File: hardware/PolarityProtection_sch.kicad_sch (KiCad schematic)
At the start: 14 parts, among them IC1 LM74502HDDFR, Q1 PSMN8R5-40MSDX

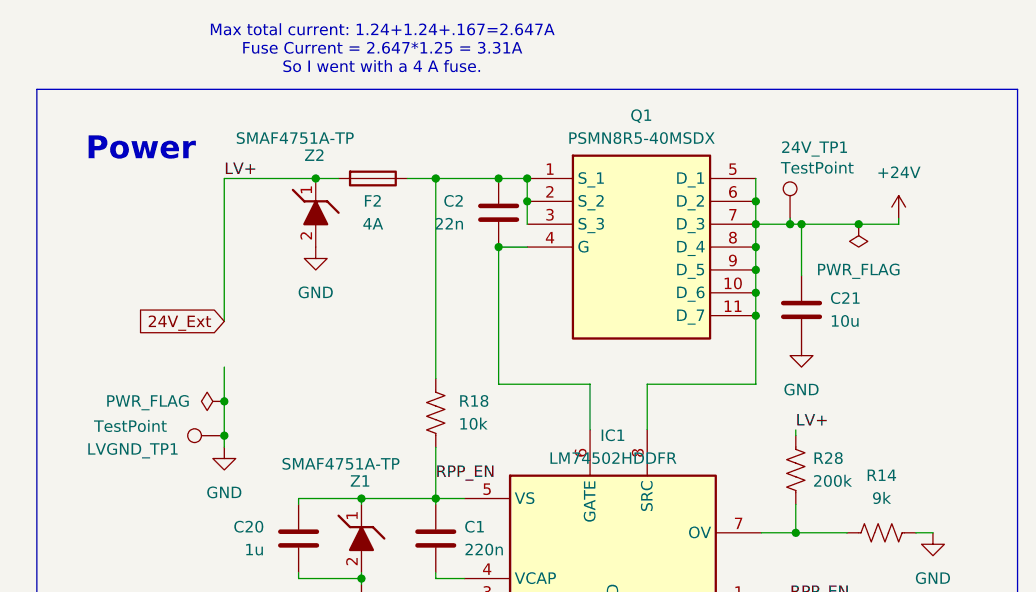
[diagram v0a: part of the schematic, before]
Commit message: Routed but having issues with gnd being pretty isolated
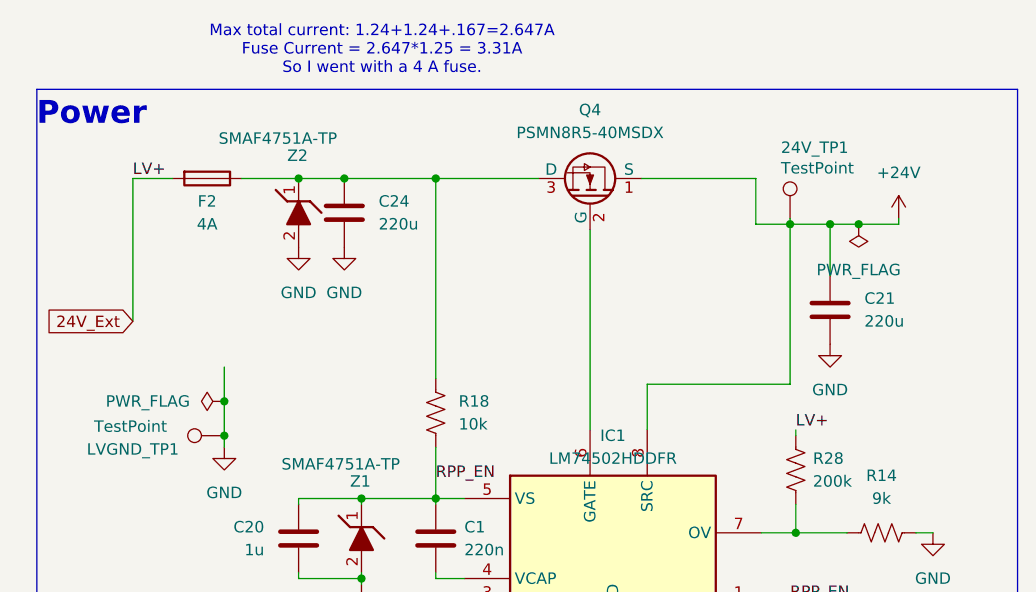
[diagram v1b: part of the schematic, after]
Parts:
- removed C2: 22n, Capacitor_SMD:C_0603_1608Metric, symbol Device:C
- removed Q1: PSMN8R5-40MSDX, UTSVT_Power:PSMN8R5-40MSDX, symbol UTSVT_Power:PSMN8R5-40MSDX
- added C24: 220u, Capacitor_SMD:C_0805_2012Metric, symbol Device:C
- added Q4: PSMN8R5-40MSDX, UTSVT_Power:PSMN8R5-40MSDX, symbol UTSVT-Power:PSMN8R5-40MSDX
- C21: value 10u -> 220u
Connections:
- net +24V: now also Q4.1 (S)
- net 24V_Ext: no longer Z2.1 (K)
- net GND: now also C24.2
- net at F2.1, R18.1: now also Z2.1 (K), C24.1, Q4.3 (D)
- net at IC1.6 (GATE): now also Q4.2 (G)
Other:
- moved on the sheet: C21, F2, Z2

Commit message: BOM
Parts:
- C1: P/N (none) -> C0603X224J5RACTU
- C20: value 1u -> 1uF; P/N (none) -> MLASU168SB5105KTNA01
- C21, C24: P/N (none) -> CL21A106KBYQNNE
- F2: P/N (none) -> 3568
- IC1: P/N (none) -> LM74502HDDFR
- Q4: P/N (none) -> PSMN8R5-40MSDX
- R14: P/N (none) -> PTN0603E9061BBT5
- R18: P/N (none) -> CRCW060310K0FKEI
- R28: P/N (none) -> MCT06030C2003FP500
- Z1, Z2: P/N (none) -> SMAF4757A-TP
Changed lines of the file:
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@@
 			)
 		)
-		(property "Description" "Unpolarized capacitor"
+		(property "Description" "Multilayer Ceramic Capacitors MLCC - SMD/SMT 50V 0.22uF X7R 125C 0603"
 			(at 122.555 92.075 0)
 			(effects
@@
 				)
 				(hide yes)
+			)
+		)
+		(property "P/N" "C0603X224J5RACTU"
+			(at 122.555 92.075 0)
+			(effects
+				(font
+					(size 1.27 1.27)
+				)
 			)
 		)
@@
 			)
 		)
-		(property "Description" "Resistor, US symbol"
+		(property "Description" "Thick Film Resistors - SMD 10K OHM 1%"
 			(at 122.555 78.105 0)
 			(effects
@@
 				)
 				(hide yes)
+			)
+		)
+		(property "P/N" "CRCW060310K0FKEI "
+			(at 122.555 78.105 0)
+			(effects
+				(font
+					(size 1.27 1.27)
+				)
 			)
 		)
@@
 			)
 		)
-		(property "Description" "Unpolarized capacitor"
+		(property "Description" "Multilayer Ceramic Capacitors MLCC - SMD/SMT 10uF 50V X5R 2012 0805"
 			(at 112.395 55.88 0)
 			(effects
@@
 				)
 				(hide yes)
+			)
+		)
+		(property "P/N" "CL21A106KBYQNNE"
+			(at 112.395 55.88 0)
+			(effects
+				(font
+					(size 1.27 1.27)
+				)
 			)
 		)
@@
 			)
 		)
-		(property "Description" "Fuse"
+		(property "Description" "THT Blade fuse holder"
 			(at 97.155 52.07 0)
 			(effects
@@
 				)
 				(hide yes)
+			)
+		)
+		(property "P/N" "3568"
+			(at 97.155 52.07 0)
+			(effects
+				(font
+					(size 1.27 1.27)
+				)
 			)
 		)
@@
 			)
 		)
-		(property "Description" "Hot Swap Voltage Controllers 3.2-V to 65-V industrial RPP controller with load disconnect, OVP, and high gate drive"
+		(property "Description" "Hot Swap Voltage Controllers 3.2-V to 65-V indust rial RPP controller"
 			(at 125.73 87.63 0)
 			(effects
@@
 				(justify left top)
 				(hide yes)
+			)
+		)
+		(property "P/N" "LM74502HDDFR"
+			(at 125.73 87.63 0)
+			(effects
+				(font
+					(size 1.27 1.27)
+				)
 			)
 		)
@@
 			)
 		)
-		(property "Description" "1.0 Watt Zener Diodes 6.2V to 100V"
+		(property "Description" "Zener Diodes ZENER DIODES,1W 51V, DO-221AC"
 			(at 107.315 49.53 0)
 			(effects
@@
 			)
 		)
+		(property "P/N" "SMAF4757A-TP"
+			(at 107.315 49.53 0)
+			(effects
+				(font
+					(size 1.27 1.27)
+				)
+			)
+		)
 		(pin "1"
 		)
@@
 			)
 		)
-		(property "Description" "1.0 Watt Zener Diodes 6.2V to 100V"
+		(property "Description" "Zener Diodes ZENER DIODES,1W 51V, DO-221AC"
 			(at 114.3 85.725 0)
 			(effects
@@
 				(justify left top)
 				(hide yes)
+			)
+		)
+		(property "P/N" "SMAF4757A-TP"
+			(at 114.3 85.725 0)
+			(effects
+				(font
+					(size 1.27 1.27)
+				)
 			)
 		)
@@
 			)
 		)
-		(property "Description" "Resistor, US symbol"
+		(property "Description" "Thin Film Resistors - SMD 9.06K OHM .1% 25PPM 1/6W"
 			(at 172.085 91.44 0)
 			(effects
@@
 				)
 				(hide yes)
+			)
+		)
+		(property "P/N" "PTN0603E9061BBT5"
+			(at 172.085 91.44 0)
+			(effects
+				(font
+					(size 1.27 1.27)
+				)
 			)
 		)
@@
 			)
 		)
-		(property "Description" "Unpolarized capacitor"
+		(property "Description" "Multilayer Ceramic Capacitors MLCC - SMD/SMT 10uF 50V X5R 2012 0805"
 			(at 166.37 66.675 0)
 			(effects
@@
 				)
 				(hide yes)
+			)
+		)
+		(property "P/N" "CL21A106KBYQNNE"
+			(at 166.37 66.675 0)
+			(effects
+				(font
+					(size 1.27 1.27)
+				)
 			)
 		)
@@
 			)
 		)
-		(property "Description" "MOSFETs PSMN8R5-40MSD/SOT1210/mLFPAK"
+		(property "Description" "MOSFETs SOT1210 N-CH 40V 60A"
 			(at 138.684 40.005 0)
 			(effects
@@
 				(justify left top)
 				(hide yes)
+			)
+		)
+		(property "P/N" "PSMN8R5-40MSDX"
+			(at 139.7 51.435 0)
+			(effects
+				(font
+					(size 1.27 1.27)
+				)
 			)
 		)
@@
 			)
 		)
-		(property "Value" "1u"
+		(property "Value" "1uF"
 			(at 103.505 93.3449 0)
 			(effects
@@
 			)
 		)
-		(property "Description" "Unpolarized capacitor"
+		(property "Description" "Multilayer Ceramic Capacitors MLCC - SMD/SMT 50V 1uF X5R 0603 10%"
 			(at 107.315 92.075 0)
 			(effects
@@
 				)
 				(hide yes)
+			)
+		)
+		(property "P/N" "MLASU168SB5105KTNA01"
+			(at 107.315 92.075 0)
+			(effects
+				(font
+					(size 1.27 1.27)
+				)
 			)
 		)
@@
 			)
 		)
-		(property "Description" "Resistor, US symbol"
+		(property "Description" "Thin Film Resistors - SMD .1W 200Kohm 1% 0603 50ppm Auto"
 			(at 162.56 84.455 0)
 			(effects
@@
 			)
 		)
+		(property "P/N" "MCT06030C2003FP500 "
+			(at 162.56 84.455 0)
+			(effects
+				(font
+					(size 1.27 1.27)
+				)
+			)
+		)

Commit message: RevA
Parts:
- F2: footprint Fuse:3588 -> Fuse:Fuseholder_Blade_Mini_Keystone_3568
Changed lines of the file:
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@@
 			)
 		)
-		(property "Footprint" "Fuse:3588"
+		(property "Footprint" "Fuse:Fuseholder_Blade_Mini_Keystone_3568"
 			(at 97.155 50.292 90)
 			(effects

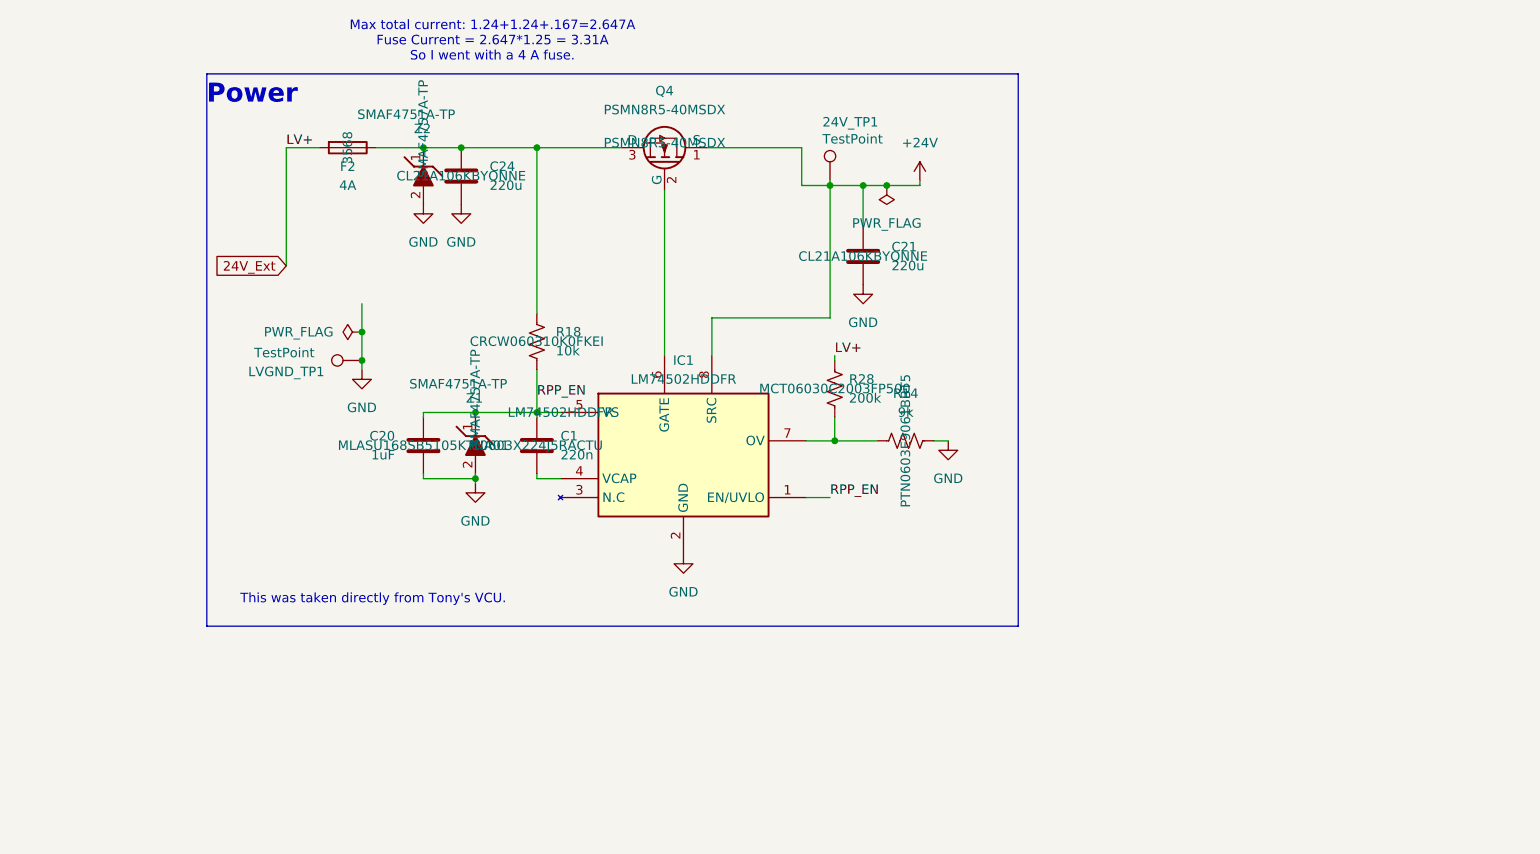
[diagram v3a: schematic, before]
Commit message: Rev B schematic Review for correct SOM connector and new IC
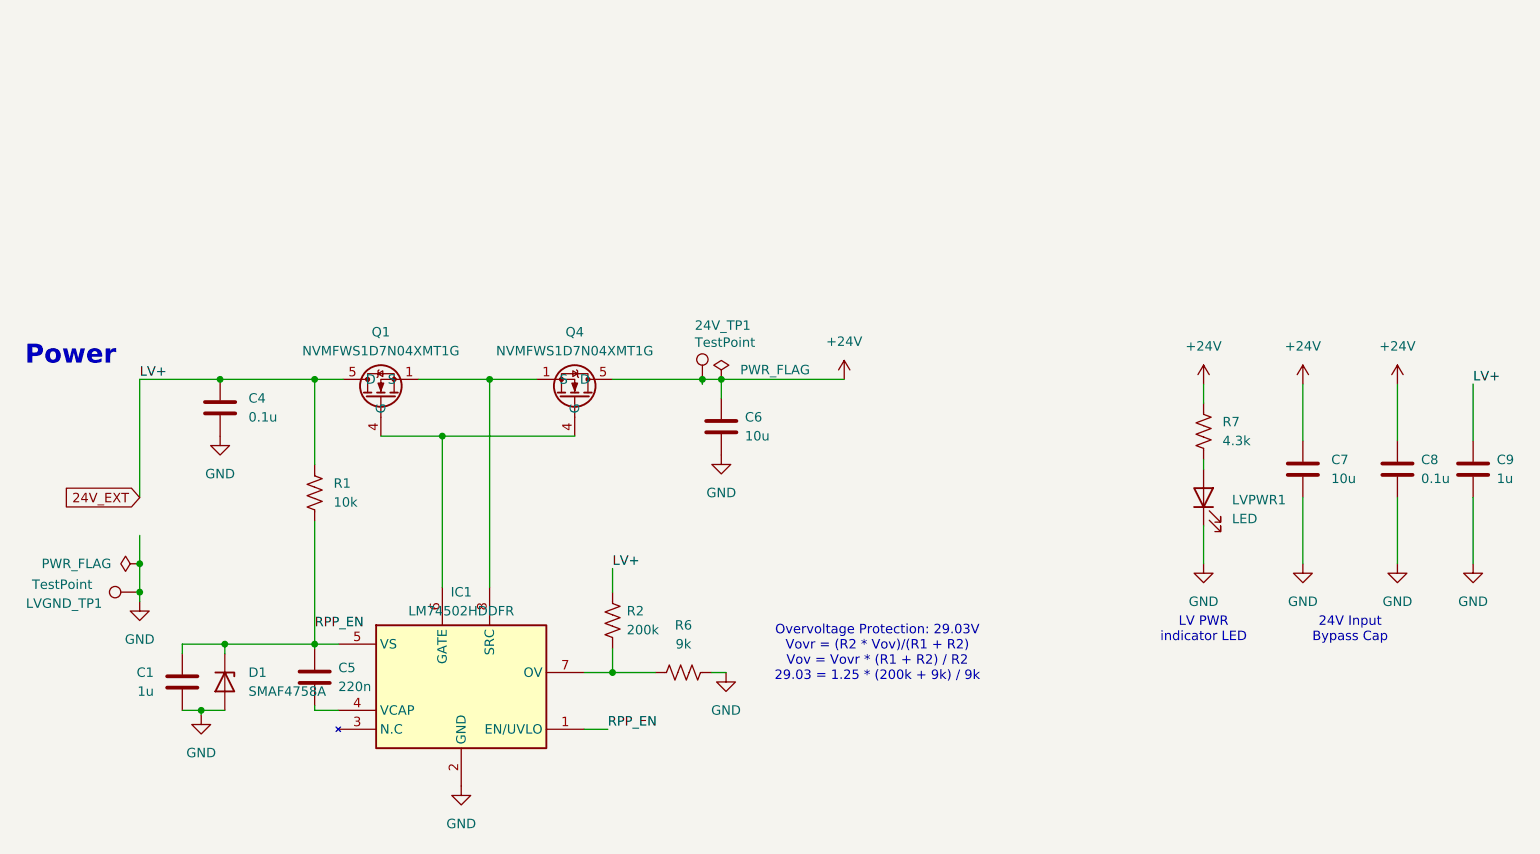
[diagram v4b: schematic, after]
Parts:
- removed C20: 1uF, Capacitor_SMD:C_0603_1608Metric, symbol Device:C
- removed C24: 220u, Capacitor_SMD:C_0805_2012Metric, symbol Device:C
- removed F2: 4A, Fuse:Fuseholder_Blade_Mini_Keystone_3568, symbol Device:Fuse
- removed Q4: PSMN8R5-40MSDX, UTSVT_Power:PSMN8R5-40MSDX, symbol UTSVT-Power:PSMN8R5-40MSDX
- removed R14: 9k, Resistor_SMD:R_0603_1608Metric, symbol Device:R_US
- removed Z1, Z2: SMAF4751A-TP, UTSVT_Passive:SODFL5026X125N, symbol UTSVT_Power:SMAF4749A-TP
- added C4, C8: 0.1u, Capacitor_SMD:C_0603_1608Metric_Pad1.08x0.95mm_HandSolder, symbol Device:C
- added C5: 220n, Capacitor_SMD:C_0603_1608Metric_Pad1.08x0.95mm_HandSolder, symbol Device:C
- added C7: 10u, Capacitor_SMD:C_0805_2012Metric_Pad1.18x1.45mm_HandSolder, symbol Device:C
- added C9: 1u, Capacitor_SMD:C_0603_1608Metric_Pad1.08x0.95mm_HandSolder, symbol Device:C
- added D1: SMAF4758A, UTSVT_Passive:SODFL5026X125N, symbol Device:D_Zener
- added LVPWR1: LED, LED_SMD:LED_0603_1608Metric_Pad1.05x0.95mm_HandSolder, symbol Device:LED
- added Q1, Q4: NVMFWS1D7N04XMT1G, UTSVT_Power:NVMFWS3D0P04M8LT1G, symbol UTSVT_Power:NVMFWS1D7N04XMT1G
- added R6: 9k, Resistor_SMD:R_0603_1608Metric_Pad0.98x0.95mm_HandSolder, symbol Device:R_US
- added R7: 4.3k, Resistor_SMD:R_0603_1608Metric_Pad0.98x0.95mm_HandSolder, symbol Device:R_US
- 24V_TP1, LVGND_TP1: footprint UTSVT_Special:TestPoint_HEX_3mmID -> TestPoint:TestPoint_Keystone_5005-5009_Compact; now left out of the parts list
- C1: value 220n -> 1u; footprint Capacitor_SMD:C_0603_1608Metric -> Capacitor_SMD:C_0603_1608Metric_Pad1.08x0.95mm_HandSolder; Mouser Part Number (none) -> 963-UMK107BJ105KA-T; P/N C0603X224J5RACTU -> UMK107BJ105KA-T
- C6: renamed from C21; value 220u -> 10u; footprint Capacitor_SMD:C_0805_2012Metric -> Capacitor_SMD:C_0805_2012Metric_Pad1.18x1.45mm_HandSolder; Mouser Part Number (none) -> 81-GRM21BR61H106KE3K; P/N CL21A106KBYQNNE -> GRM21BR61H106KE43K
- R1: renamed from R18; footprint Resistor_SMD:R_0603_1608Metric -> Resistor_SMD:R_0603_1608Metric_Pad0.98x0.95mm_HandSolder; Mouser Part Number (none) -> 71-CRCW060310K0FKEI; P/N CRCW060310K0FKEI -> CRCW060310K0FKEI
- R2: renamed from R28; footprint Resistor_SMD:R_0603_1608Metric -> Resistor_SMD:R_0603_1608Metric_Pad0.98x0.95mm_HandSolder; Mouser Part Number (none) -> 594-MCT06030C2003FP5; P/N MCT06030C2003FP500 -> MCT06030C2003FP500
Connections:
- net 24V_Ext is gone; now on net 24V_EXT: R2.1
- net +24V: now also C7.1, C8.1, Q4.5 (D), Q4.6 (D), Q4.7 (D), Q4.8 (D), Q4.9 (D), R7.1; no longer IC1.8 (SRC)
- net GND: now also C1.1, C4.2, C7.2, C8.2, C9.2, D1.2 (A), LVPWR1.1 (K), R6.2
- net RPP_EN: now also C1.2, C5.1, D1.1 (K); no longer C1.1
- net at IC1.4 (VCAP): now also C5.2; no longer C1.2
- net 24V_EXT: now reaches R1.1
- net 24V_EXT: now also C4.1, C9.1, Q1.5 (D), Q1.6 (D), Q1.7 (D), Q1.8 (D), Q1.9 (D)
- net at IC1.6 (GATE): now also Q1.4 (G), Q4.4 (G)
- net at IC1.7 (OV), R2.2: now also R6.1
- new net: IC1.8 (SRC), Q1.1 (S), Q1.2 (S), Q1.3 (S), Q4.1 (S), Q4.2 (S), Q4.3 (S)
- new net: LVPWR1.2 (A), R7.2
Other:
- note added: "24V Input Bypass Cap"
- note added: "LV PWR indicator LED"
- note added: "Overvoltage Protection: 29.03V Vovr = (R2 * Vov)/(R1 + R2) Vov = Vovr * (R1 + R2) / R2 29.03 = 1.25 * (200k + 9k) / 9k"
- note removed: "Max total current: 1.24+1.24+.167=2.647A Fuse Current = 2.647*1.25 = 3.31A So I went with a 4 A fuse."
- note removed: "This was taken directly from Tony's VCU."
- moved on the sheet: 24V_TP1, C6, IC1, LVGND_TP1, R1, R2

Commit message: Rev B schematic Review with new IC
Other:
- moved on the sheet: C1, C4, C6, C7, C8, C9, D1, IC1, LVGND_TP1, Q1, Q4, R1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
